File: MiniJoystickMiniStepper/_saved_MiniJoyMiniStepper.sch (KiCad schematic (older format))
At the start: 21 parts, among them J1 STEPPER_UNI_5P, J10 TH_0.1_1x1, J11 TH_0.1_1x1, J2 STEPPER_UNI_5P, J28 TH_0.1_1x1, J29 TH_0.1_1x1, J50 STEPPER_UNI_5P, J51 STEPPER_UNI_5P, J6 TH_0.1_1x1, J7 TH_0.1_1x1, J8 TH_0.1_1x1, J9 TH_0.1_1x1, U1 ADAFRUIT_FEATHER_M0

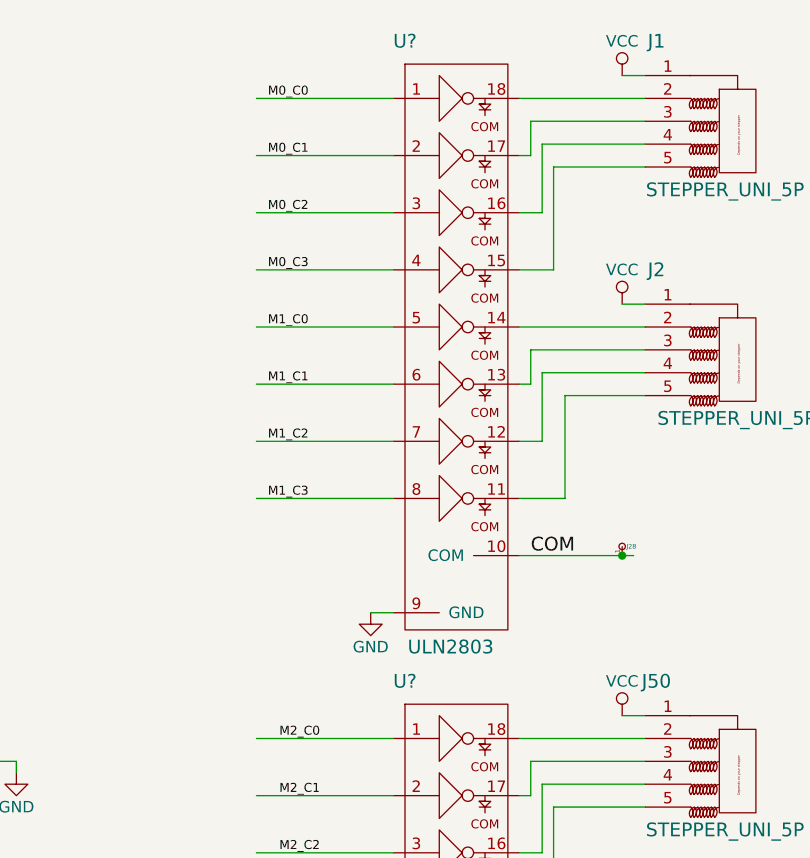
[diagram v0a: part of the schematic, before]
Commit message: Initial Placement. Some routing.
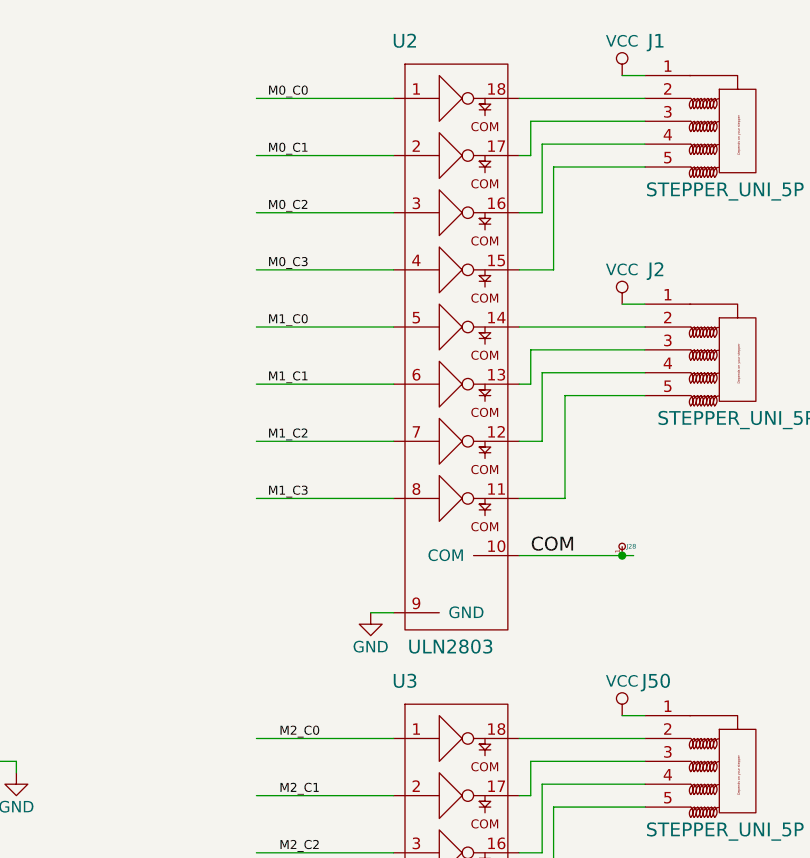
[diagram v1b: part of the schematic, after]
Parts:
- gave numbers to parts that had none: 2
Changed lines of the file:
@@
 $EndComp
 $Comp
-L GND #PWR01
+L GND #PWR2
 U 1 1 58686266
 P 1100 1600
-F 0 "#PWR01" H 1100 1350 50  0001 C CNN
+F 0 "#PWR2" H 1100 1350 50  0001 C CNN
 F 1 "GND" H 1100 1450 50  0000 C CNN
 F 2 "" H 1100 1600 50  0000 C CNN
@@
 $EndComp
 $Comp
-L VCC #PWR02
+L VCC #PWR1
 U 1 1 586863B2
 P 1100 800
-F 0 "#PWR02" H 1100 650 50  0001 C CNN
+F 0 "#PWR1" H 1100 650 50  0001 C CNN
 F 1 "VCC" H 1100 950 50  0000 C CNN
 F 2 "" H 1100 800 50  0000 C CNN
@@
 $EndComp
 $Comp
-L VCC #PWR03
+L VCC #PWR12
 U 1 1 58686699
 P 10300 850
-F 0 "#PWR03" H 10300 700 50  0001 C CNN
+F 0 "#PWR12" H 10300 700 50  0001 C CNN
 F 1 "VCC" H 10300 1000 50  0000 C CNN
 F 2 "" H 10300 850 50  0000 C CNN
@@
 $EndComp
 $Comp
-L VCC #PWR04
+L VCC #PWR14
 U 1 1 5868676D
 P 10300 3650
-F 0 "#PWR04" H 10300 3500 50  0001 C CNN
+F 0 "#PWR14" H 10300 3500 50  0001 C CNN
 F 1 "VCC" H 10300 3800 50  0000 C CNN
 F 2 "" H 10300 3650 50  0000 C CNN
@@
 $EndComp
 $Comp
-L VCC #PWR05
+L VCC #PWR15
 U 1 1 58686796
 P 10300 4650
-F 0 "#PWR05" H 10300 4500 50  0001 C CNN
+F 0 "#PWR15" H 10300 4500 50  0001 C CNN
 F 1 "VCC" H 10300 4800 50  0000 C CNN
 F 2 "" H 10300 4650 50  0000 C CNN
@@
 COM
 $Comp
-L GND #PWR06
+L GND #PWR11
 U 1 1 58686D5D
 P 9200 3200
-F 0 "#PWR06" H 9200 2950 50  0001 C CNN
+F 0 "#PWR11" H 9200 2950 50  0001 C CNN
 F 1 "GND" H 9200 3050 50  0000 C CNN
 F 2 "" H 9200 3200 50  0000 C CNN
@@
 $EndComp
 $Comp
-L GND #PWR07
+L GND #PWR10
 U 1 1 58686D89
 P 9100 6050
-F 0 "#PWR07" H 9100 5800 50  0001 C CNN
+F 0 "#PWR10" H 9100 5800 50  0001 C CNN
 F 1 "GND" H 9100 5900 50  0000 C CNN
 F 2 "" H 9100 6050 50  0000 C CNN
@@
 $EndComp
 $Comp
-L GND #PWR08
+L GND #PWR6
 U 1 1 58686DB5
 P 1850 5750
-F 0 "#PWR08" H 1850 5500 50  0001 C CNN
+F 0 "#PWR6" H 1850 5500 50  0001 C CNN
 F 1 "GND" H 1850 5600 50  0000 C CNN
 F 2 "" H 1850 5750 50  0000 C CNN
@@
 $EndComp
 $Comp
-L GND #PWR09
+L GND #PWR5
 U 1 1 58686DE1
 P 1800 3200
-F 0 "#PWR09" H 1800 2950 50  0001 C CNN
+F 0 "#PWR5" H 1800 2950 50  0001 C CNN
 F 1 "GND" H 1800 3050 50  0000 C CNN
 F 2 "" H 1800 3200 50  0000 C CNN
@@
 $EndComp
 $Comp
-L VCC #PWR010
+L VCC #PWR3
 U 1 1 58686E65
 P 1750 2050
-F 0 "#PWR010" H 1750 1900 50  0001 C CNN
+F 0 "#PWR3" H 1750 1900 50  0001 C CNN
 F 1 "VCC" H 1750 2200 50  0000 C CNN
 F 2 "" H 1750 2050 50  0000 C CNN
@@
 $EndComp
 $Comp
-L VCC #PWR011
+L VCC #PWR4
 U 1 1 58686F85
 P 1750 4600
-F 0 "#PWR011" H 1750 4450 50  0001 C CNN
+F 0 "#PWR4" H 1750 4450 50  0001 C CNN
 F 1 "VCC" H 1750 4750 50  0000 C CNN
 F 2 "" H 1750 4600 50  0000 C CNN
@@
 Connection ~ 4400 1350
 $Comp
-L GND #PWR012
+L GND #PWR8
 U 1 1 586B2C75
 P 5050 2650
-F 0 "#PWR012" H 5050 2400 50  0001 C CNN
+F 0 "#PWR8" H 5050 2400 50  0001 C CNN
 F 1 "GND" H 5050 2500 50  0000 C CNN
 F 2 "" H 5050 2650 50  0000 C CNN
@@
 Connection ~ 5050 2500
 $Comp
-L GND #PWR013
+L GND #PWR7
 U 1 1 586B6627
 P 4700 4650
-F 0 "#PWR013" H 4700 4400 50  0001 C CNN
+F 0 "#PWR7" H 4700 4400 50  0001 C CNN
 F 1 "GND" H 4700 4500 50  0000 C CNN
 F 2 "" H 4700 4650 50  0000 C CNN
@@
 $EndComp
 $Comp
-L GND #PWR014
+L GND #PWR9
 U 1 1 586B66E6
 P 7650 3900
-F 0 "#PWR014" H 7650 3650 50  0001 C CNN
+F 0 "#PWR9" H 7650 3650 50  0001 C CNN
 F 1 "GND" H 7650 3750 50  0000 C CNN
 F 2 "" H 7650 3900 50  0000 C CNN
@@
 $EndComp
 $Comp
-L VCC #PWR015
+L VCC #PWR13
 U 1 1 586866C2
 P 10300 1850
-F 0 "#PWR015" H 10300 1700 50  0001 C CNN
+F 0 "#PWR13" H 10300 1700 50  0001 C CNN
 F 1 "VCC" H 10300 2000 50  0000 C CNN
 F 2 "" H 10300 1850 50  0000 C CNN
@@
 	8700 1950 9300 1950
 $Comp
-L ULN2803 U?
+L ULN2803 U2
 U 1 1 586C241A
 P 9500 1850
-F 0 "U?" H 9350 3000 60  0000 C CNN
+F 0 "U2" H 9350 3000 60  0000 C CNN
 F 1 "ULN2803" H 9550 350 60  0000 C CNN
 F 2 "" H 9550 2200 60  0001 C CNN
@@
 $EndComp
 $Comp
-L ULN2803 U?
+L ULN2803 U3
 U 1 1 586C2749
 P 9500 4650
-F 0 "U?" H 9350 5800 60  0000 C CNN
+F 0 "U3" H 9350 5800 60  0000 C CNN
 F 1 "ULN2803" H 9550 3150 60  0000 C CNN
 F 2 "" H 9550 5000 60  0001 C CNN
